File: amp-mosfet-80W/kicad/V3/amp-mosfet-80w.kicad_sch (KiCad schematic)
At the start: 60 parts, among them J1 Conn_01x01, J2 Conn_01x01, J3 +50V, J4 -50V, J5 LS+, J6 LS-, J7 GND, Q1 BC856BS, Q11 ECX10P20, Q12 ECX10N20, Q2 BC856BS, Q3 DZT5551, Q4 DZT5401, Q5 DZT5401, Q6 DZT5551

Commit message: WIP
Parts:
- removed C17: 470p, Capacitor_SMD:C_0805_2012Metric_Pad1.18x1.45mm_HandSolder, symbol Device:C
- removed Q3: DZT5551, Package_TO_SOT_SMD:SOT-223-3_TabPin2, symbol kicad-snk:DZT5551
- removed Q4: DZT5401, Package_TO_SOT_SMD:SOT-223-3_TabPin2, symbol kicad-snk:DZT5401
- added Q3: BC856BS, Package_TO_SOT_SMD:SOT-363_SC-70-6, symbol Transistor_BJT:BC856BS
- added Q4: BC846BDW1, Package_TO_SOT_SMD:SOT-363_SC-70-6, symbol Transistor_BJT:BC846BDW1
- added Q7: BC856B, Package_TO_SOT_SMD:SOT-23, symbol Transistor_BJT:BC856
- added Q8: BC846, Package_TO_SOT_SMD:SOT-23, symbol Transistor_BJT:BC846
- added R13: 1k, Resistor_SMD:R_0805_2012Metric_Pad1.20x1.40mm_HandSolder, symbol Device:R
- added R15, R22: 100R, Resistor_SMD:R_0805_2012Metric_Pad1.20x1.40mm_HandSolder, symbol Device:R
- added R16: 22k, Resistor_SMD:R_0805_2012Metric_Pad1.20x1.40mm_HandSolder, symbol Device:R
- added R23, R24: 2.2k, Resistor_SMD:R_0805_2012Metric_Pad1.20x1.40mm_HandSolder, symbol Device:R
- added R25: 33R, Resistor_SMD:R_0805_2012Metric_Pad1.20x1.40mm_HandSolder, symbol Device:R
- C1: value 2.2uF -> 3.3uF
- C3: value 10n -> 47p; footprint Capacitor_THT:C_Rect_L7.2mm_W2.5mm_P5.00mm_FKS2_FKP2_MKS2_MKP2 -> Capacitor_SMD:C_0805_2012Metric_Pad1.18x1.45mm_HandSolder
- C8: value 18p -> 47p
- R12: value 100R -> 220R
- R20: value 100R -> 33R
- R4, R7: value 3k9 -> 1k
- R5: value 430R -> 220R
- R6: value 22k -> 100R
- R8: value 100R -> 1k
- R9: value 12k/1W -> 100R; footprint Resistor_SMD:R_1206_3216Metric_Pad1.30x1.75mm_HandSolder -> Resistor_SMD:R_0805_2012Metric_Pad1.20x1.40mm_HandSolder
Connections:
- net GND: now also Q7.3 (C), R16.2
- net at C2.1, Q1.2 (B1), R2.1: now also Q3.5 (B2)
- net at Q2.6 (C1), R6.1: now also R22.1
- net at Q1.1 (E1), R6.2: no longer Q1.4 (E2)
- net at C11.1, C9.1, Q2.4 (E2)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: now also R8.2, R13.2, R23.1; no longer R8.1
- net at C5.2, Q1.5 (B2), R10.1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: now also Q3.2 (B1)
- net at C10.2, C12.2, R18.2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: now also R12.1, Q4.4 (E2), R24.2, R25.2; no longer R12.2
- net at Q1.6 (C1), R4.1: now also C8.2, Q8.1 (B); no longer C8.1, Q6.1 (B)
- net at C3.2: now also R8.1, Q3.3 (C2), Q7.1 (B); no longer R9.2
- net at C7.2, D1.2 (A), Q5.2 (C)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: now also C3.1
- net at C7.1, D4.2 (A), Q6.2 (C)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: now also C8.1; no longer C8.2
- net at Q6.3 (E): now also R25.1; no longer R12.1
- new net: Q1.4 (E2), R22.2
- new net: Q5.1 (B), Q7.2 (E), R23.2
- new net: Q6.1 (B), Q8.2 (E), R24.1
- new net: Q3.1 (E1), R15.2
- new net: Q3.6 (C1), R13.1
- new net: Q4.2 (B1), Q4.3 (C2), R16.1
- new net: Q4.1 (E1), Q4.5 (B2), R12.2
- new net: Q3.4 (E2), R9.2
- new net: Q4.6 (C1), R15.1, R9.1
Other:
- note added: "I:3.1MA"
- note removed: "C17: do not populate"
- note removed: "I:1.7mA = > 430R"
- moved on the sheet: C10, C11, C12, C13, C14, C18, C4, C5, C6, C7, C9, D1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

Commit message: WIP
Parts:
- removed JP1, JP2: Jump, Connector_PinHeader_2.54mm:PinHeader_1x02_P2.54mm_Vertical, symbol Jumper:Jumper_2_Bridged
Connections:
- net GND: now also Q8.3 (C)
- net at D5.2 (A): now also C14.1, J3.1 (Pin_1), Q12.3 (D)
- net at C18.2, J4.1 (Pin_1), Q11.3 (S): now also D6.1 (K)
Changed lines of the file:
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@@
     (stroke (width 0) (type default) (color 0 0 0 0))
   )
-  (wire (pts (xy 317.5 217.17) (xy 335.28 217.17))
+  (wire (pts (xy 306.07 217.17) (xy 335.28 217.17))
     (stroke (width 0) (type default) (color 0 0 0 0))
   )
@@
     (stroke (width 0) (type default) (color 0 0 0 0))
   )
+  (wire (pts (xy 237.49 179.07) (xy 237.49 180.34))
+    (stroke (width 0) (type default) (color 0 0 0 0))
+  )
   (wire (pts (xy 287.02 58.42) (xy 287.02 60.96))
     (stroke (width 0) (type default) (color 0 0 0 0))
@@
     (stroke (width 0) (type default) (color 0 0 0 0))
   )
-  (wire (pts (xy 306.07 58.42) (xy 307.34 58.42))
-    (stroke (width 0) (type default) (color 0 0 0 0))
-  )
   (wire (pts (xy 248.92 166.37) (xy 248.92 171.45))
     (stroke (width 0) (type default) (color 0 0 0 0))
@@
     (stroke (width 0) (type default) (color 0 0 0 0))
   )
-  (wire (pts (xy 317.5 58.42) (xy 335.28 58.42))
+  (wire (pts (xy 306.07 58.42) (xy 335.28 58.42))
     (stroke (width 0) (type default) (color 0 0 0 0))
   )
@@
   )
   (wire (pts (xy 165.1 151.13) (xy 165.1 149.86))
-    (stroke (width 0) (type default) (color 0 0 0 0))
-  )
-  (wire (pts (xy 307.34 217.17) (xy 306.07 217.17))
     (stroke (width 0) (type default) (color 0 0 0 0))
   )
@@
     (pin "1")
   )
-  (symbol (lib_id "Jumper:Jumper_2_Bridged") (at 312.42 58.42 0) (unit 1)
-    (in_bom yes) (on_board yes)
-    (property "Reference" "JP1" (id 0) (at 312.42 53.467 0))
-    (property "Value" "Jump" (id 1) (at 312.42 55.7784 0))
-    (property "Footprint" "Connector_PinHeader_2.54mm:PinHeader_1x02_P2.54mm_Vertical" (id 2) (at 312.42 58.42 0)
-      (effects (font (size 1.27 1.27)) hide)
-    )
-    (property "Datasheet" "~" (id 3) (at 312.42 58.42 0)
-      (effects (font (size 1.27 1.27)) hide)
-    )
-    (pin "1")
-    (pin "2")
-  )
   (symbol (lib_id "Device:R") (at 156.21 64.77 0) (unit 1)
     (in_bom yes) (on_board yes)
@@
     )
     (property "Datasheet" "~" (id 3) (at 156.21 64.77 0)
-      (effects (font (size 1.27 1.27)) hide)
-    )
-    (pin "1")
-    (pin "2")
-  )
-  (symbol (lib_id "Jumper:Jumper_2_Bridged") (at 312.42 217.17 180) (unit 1)
-    (in_bom yes) (on_board yes)
-    (property "Reference" "JP2" (id 0) (at 312.42 211.455 0))
-    (property "Value" "Jump" (id 1) (at 312.42 213.7664 0))
-    (property "Footprint" "Connector_PinHeader_2.54mm:PinHeader_1x02_P2.54mm_Vertical" (id 2) (at 312.42 217.17 0)
-      (effects (font (size 1.27 1.27)) hide)
-    )
-    (property "Datasheet" "~" (id 3) (at 312.42 217.17 0)
       (effects (font (size 1.27 1.27)) hide)
     )
@@
       (reference "J7") (unit 1) (value "GND") (footprint "Connector_Wire:SolderWire-1.5sqmm_1x01_D1.7mm_OD3.9mm")
     )
-    (path "/00000000-0000-0000-0000-000061924f3d"
-      (reference "JP1") (unit 1) (value "Jump") (footprint "Connector_PinHeader_2.54mm:PinHeader_1x02_P2.54mm_Vertical")
-    )
-    (path "/00000000-0000-0000-0000-000061925756"
-      (reference "JP2") (unit 1) (value "Jump") (footprint "Connector_PinHeader_2.54mm:PinHeader_1x02_P2.54mm_Vertical")
-    )
     (path "/00000000-0000-0000-0000-00006196da4b"

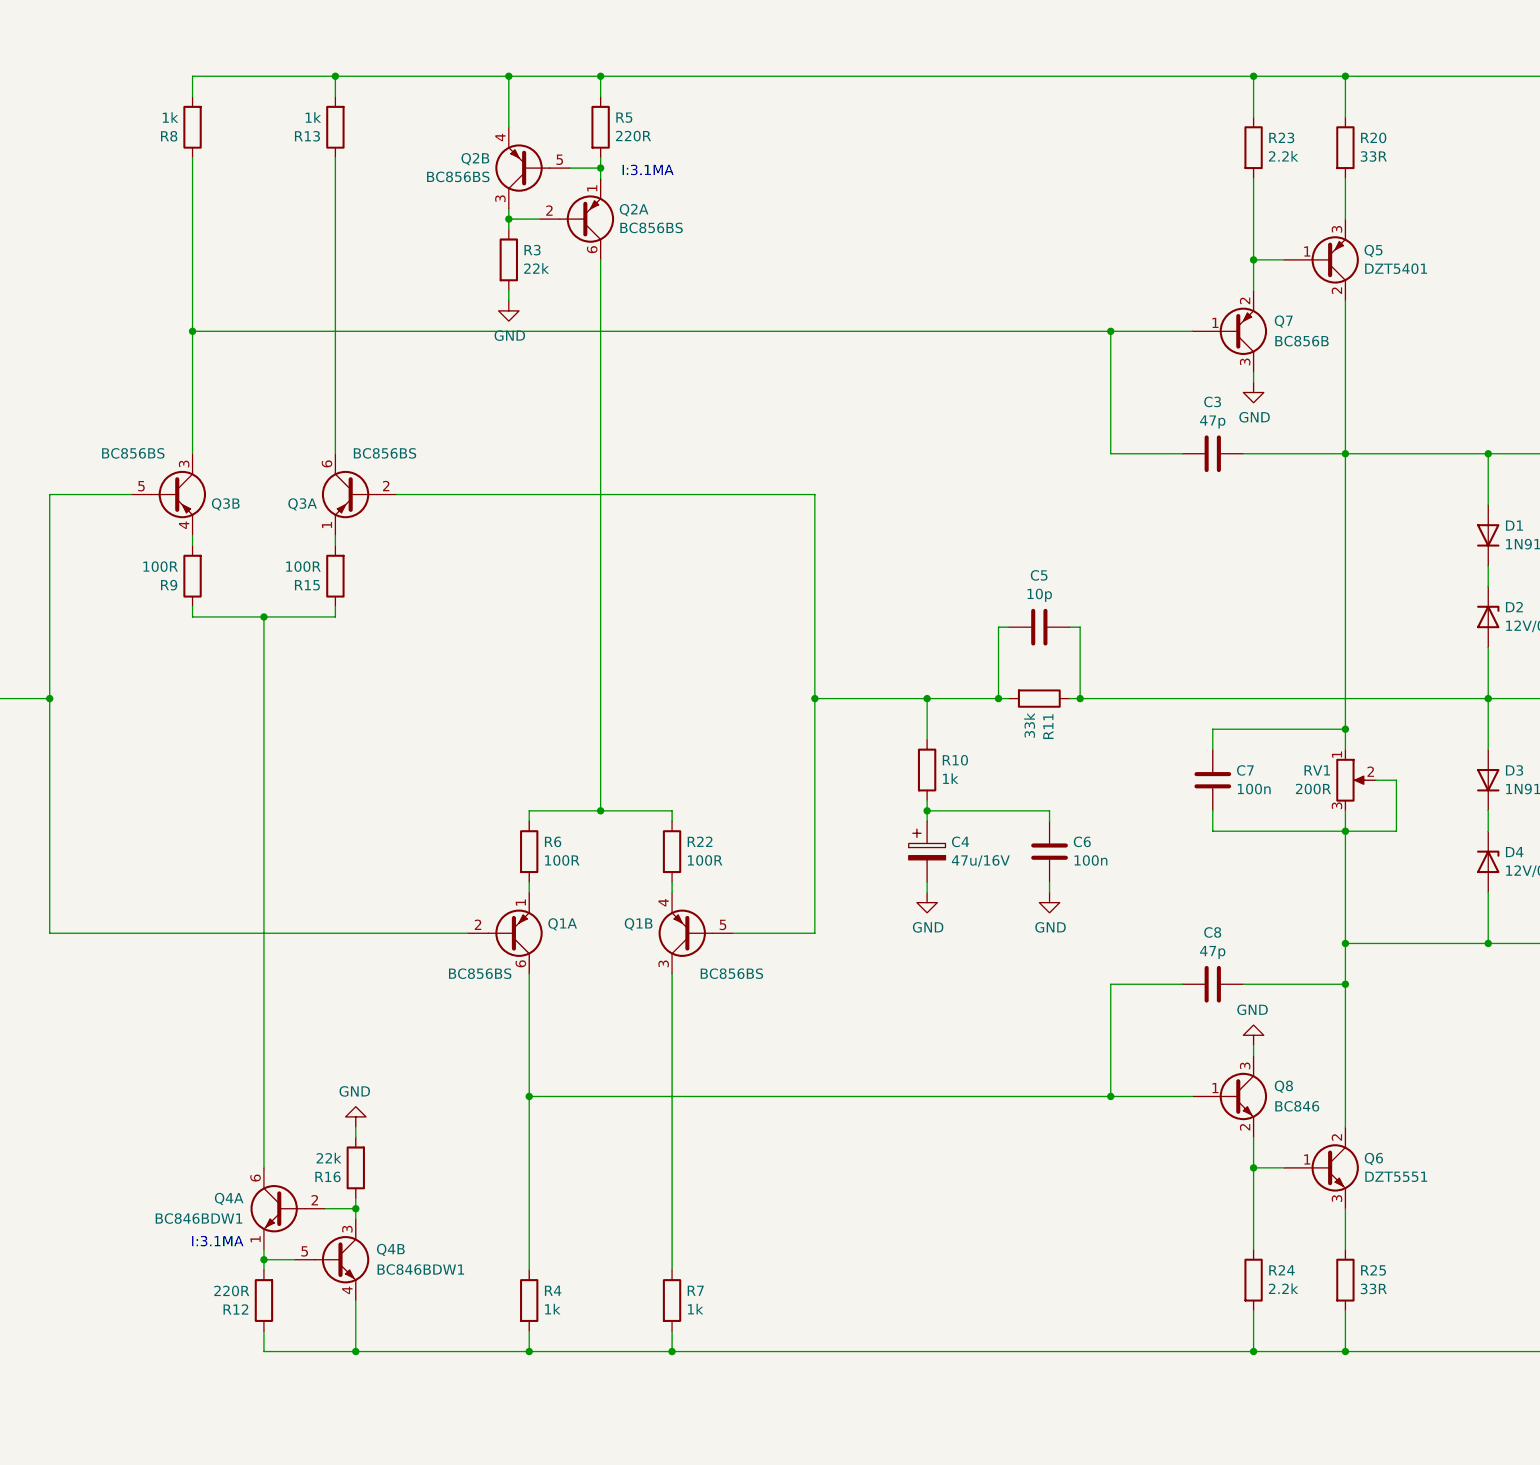
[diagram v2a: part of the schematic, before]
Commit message: Update amp-mosfet-80w.kicad_sch
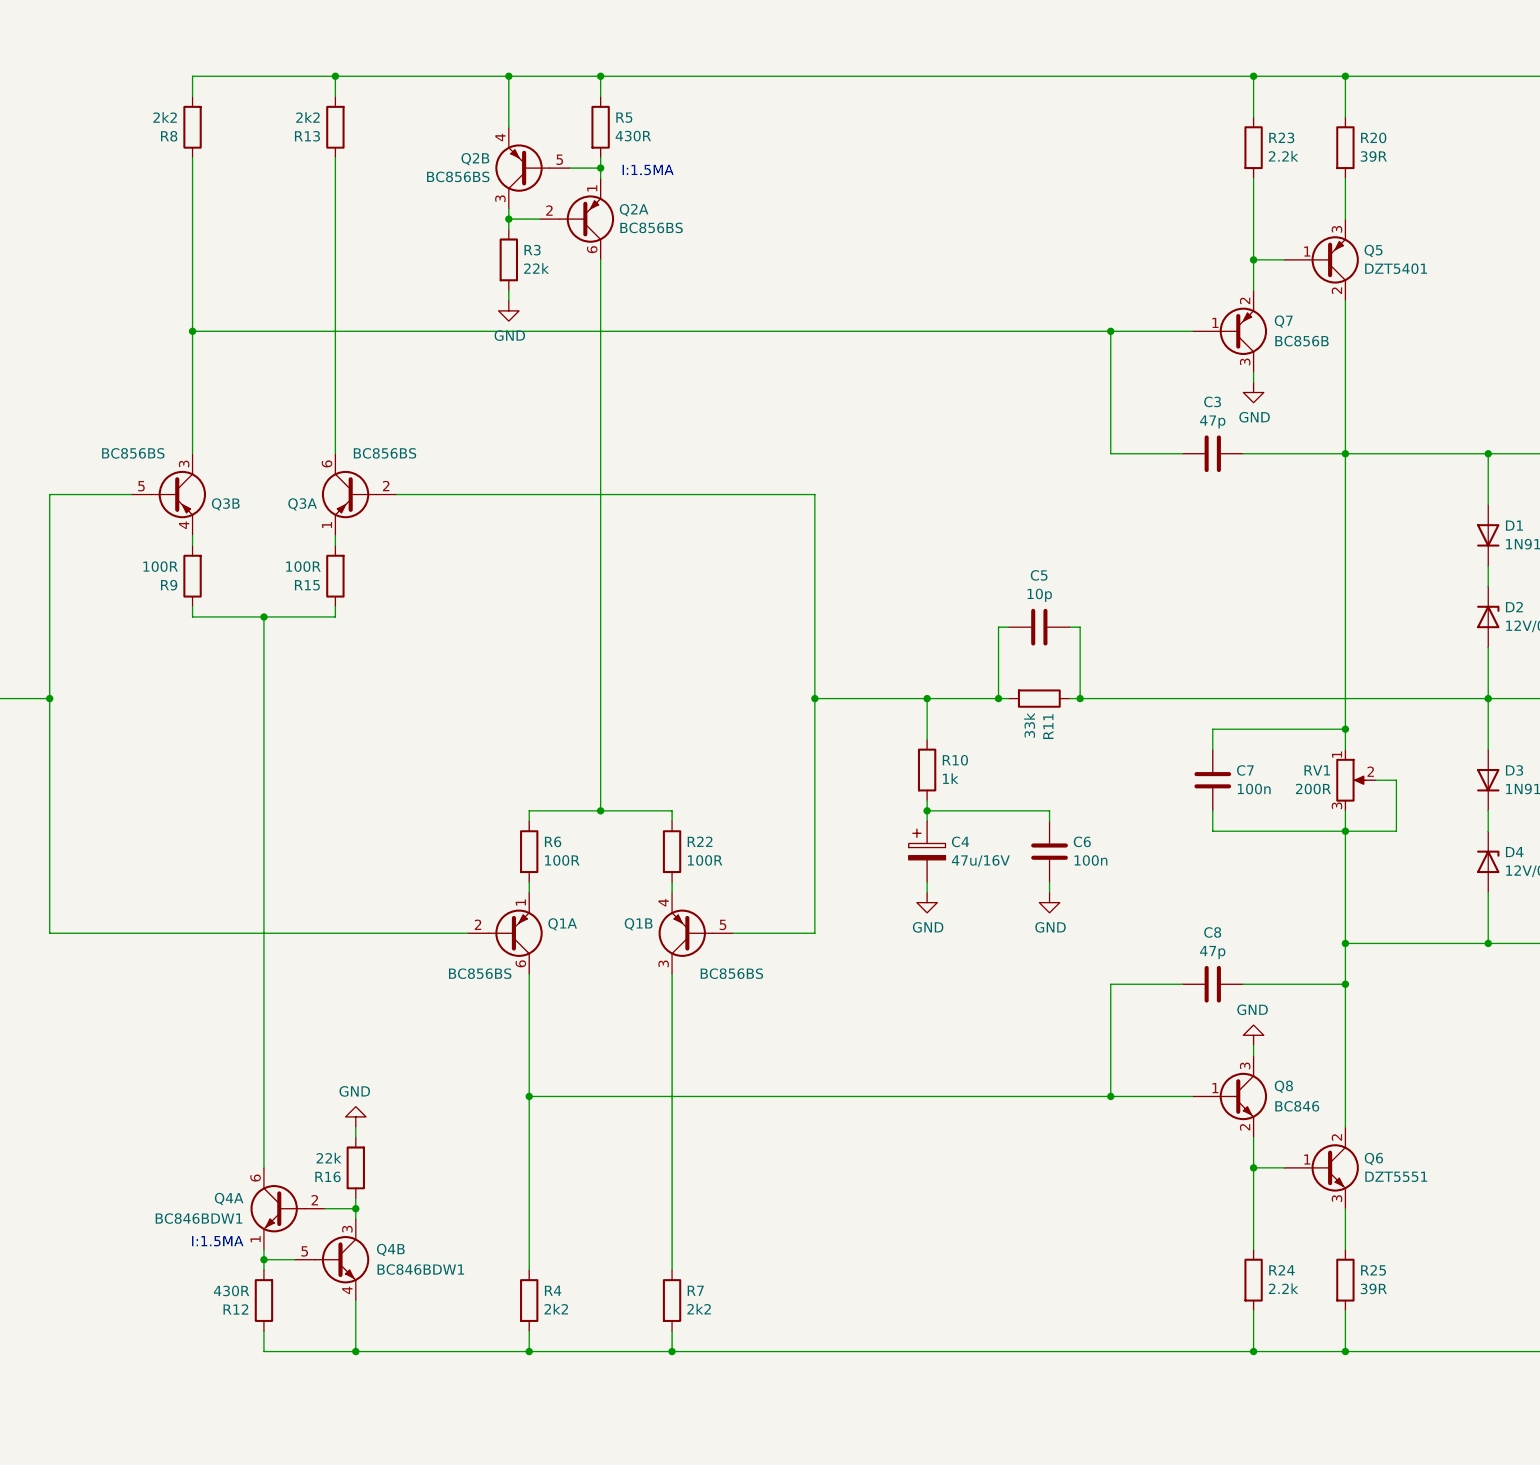
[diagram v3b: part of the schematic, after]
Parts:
- R12, R5: value 220R -> 430R
- R13, R4, R7, R8: value 1k -> 2k2
- R20, R25: value 33R -> 39R
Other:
- note added: "I:1.5MA"
- note removed: "I:3.1MA"
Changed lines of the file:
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@@
   (title_block
     (title "Lateral MOS FET 80W")
-    (date "2021-12-30")
+    (date "2022-01-07")
     (rev "V3")
   )
@@
     (stroke (width 0) (type default) (color 0 0 0 0))
   )
-  (text "I:3.1MA" (at 111.76 204.47 180)
+  (text "I:1.5MA" (at 111.76 204.47 180)
     (effects (font (size 1.27 1.27)) (justify right bottom))
   )
@@
     (effects (font (size 1.27 1.27)) (justify left bottom))
   )
-  (text "I:3.1MA" (at 158.75 71.12 0)
+  (text "I:1.5MA" (at 158.75 71.12 0)
     (effects (font (size 1.27 1.27)) (justify left bottom))
   )
@@
       (effects (font (size 1.27 1.27)) (justify left))
     )
-    (property "Value" "220R" (id 1) (at 157.988 65.913 0)
+    (property "Value" "430R" (id 1) (at 157.988 65.913 0)
       (effects (font (size 1.27 1.27)) (justify left))
     )
@@
       (effects (font (size 1.27 1.27)) (justify left))
     )
-    (property "Value" "1k" (id 1) (at 166.878 211.963 0)
+    (property "Value" "2k2" (id 1) (at 166.878 211.963 0)
       (effects (font (size 1.27 1.27)) (justify left))
     )
@@
       (effects (font (size 1.27 1.27)) (justify left))
     )
-    (property "Value" "1k" (id 1) (at 149.098 211.963 0)
+    (property "Value" "2k2" (id 1) (at 149.098 211.963 0)
       (effects (font (size 1.27 1.27)) (justify left))
     )
@@
       (effects (font (size 1.27 1.27)) (justify left))
     )
-    (property "Value" "33R" (id 1) (at 250.698 68.453 0)
+    (property "Value" "39R" (id 1) (at 250.698 68.453 0)
       (effects (font (size 1.27 1.27)) (justify left))
     )
@@
       (effects (font (size 1.27 1.27)) (justify left))
     )
-    (property "Value" "33R" (id 1) (at 250.698 209.423 0)
+    (property "Value" "39R" (id 1) (at 250.698 209.423 0)
       (effects (font (size 1.27 1.27)) (justify left))
     )
@@
       (effects (font (size 1.27 1.27)) (justify left))
     )
-    (property "Value" "1k" (id 1) (at 121.412 63.627 0)
+    (property "Value" "2k2" (id 1) (at 121.412 63.627 0)
       (effects (font (size 1.27 1.27)) (justify left))
     )
@@
       (effects (font (size 1.27 1.27)) (justify left))
     )
-    (property "Value" "1k" (id 1) (at 103.632 63.627 0)
+    (property "Value" "2k2" (id 1) (at 103.632 63.627 0)
       (effects (font (size 1.27 1.27)) (justify left))
     )
@@
       (effects (font (size 1.27 1.27)) (justify left))
     )
-    (property "Value" "220R" (id 1) (at 112.522 209.677 0)
+    (property "Value" "430R" (id 1) (at 112.522 209.677 0)
       (effects (font (size 1.27 1.27)) (justify left))
     )
@@
     )
     (path "/00000000-0000-0000-0000-000061935443"
-      (reference "R4") (unit 1) (value "1k") (footprint "Resistor_SMD:R_0805_2012Metric_Pad1.20x1.40mm_HandSolder")
+      (reference "R4") (unit 1) (value "2k2") (footprint "Resistor_SMD:R_0805_2012Metric_Pad1.20x1.40mm_HandSolder")
     )
     (path "/00000000-0000-0000-0000-00006192531f"
-      (reference "R5") (unit 1) (value "220R") (footprint "Resistor_SMD:R_0805_2012Metric_Pad1.20x1.40mm_HandSolder")
+      (reference "R5") (unit 1) (value "430R") (footprint "Resistor_SMD:R_0805_2012Metric_Pad1.20x1.40mm_HandSolder")
     )
     (path "/00000000-0000-0000-0000-00006191f500"
@@
     )
     (path "/00000000-0000-0000-0000-000061934148"
-      (reference "R7") (unit 1) (value "1k") (footprint "Resistor_SMD:R_0805_2012Metric_Pad1.20x1.40mm_HandSolder")
+      (reference "R7") (unit 1) (value "2k2") (footprint "Resistor_SMD:R_0805_2012Metric_Pad1.20x1.40mm_HandSolder")
     )
     (path "/bc4f73f6-106f-4cc8-bb82-bc8efa1afc3e"
-      (reference "R8") (unit 1) (value "1k") (footprint "Resistor_SMD:R_0805_2012Metric_Pad1.20x1.40mm_HandSolder")
+      (reference "R8") (unit 1) (value "2k2") (footprint "Resistor_SMD:R_0805_2012Metric_Pad1.20x1.40mm_HandSolder")
     )
     (path "/df83a6e7-4009-4e15-8848-71fca1944547"
@@
     )
     (path "/cc4b2573-d454-4623-b5a2-500c7c0c1f4f"
-      (reference "R12") (unit 1) (value "220R") (footprint "Resistor_SMD:R_0805_2012Metric_Pad1.20x1.40mm_HandSolder")
+      (reference "R12") (unit 1) (value "430R") (footprint "Resistor_SMD:R_0805_2012Metric_Pad1.20x1.40mm_HandSolder")
     )
     (path "/6a7d600b-c6ab-4f20-9356-09f2372162be"
-      (reference "R13") (unit 1) (value "1k") (footprint "Resistor_SMD:R_0805_2012Metric_Pad1.20x1.40mm_HandSolder")
+      (reference "R13") (unit 1) (value "2k2") (footprint "Resistor_SMD:R_0805_2012Metric_Pad1.20x1.40mm_HandSolder")
     )
     (path "/00000000-0000-0000-0000-00006195ccda"
@@
     )
     (path "/00000000-0000-0000-0000-0000619d631c"
-      (reference "R20") (unit 1) (value "33R") (footprint "Resistor_SMD:R_0805_2012Metric_Pad1.20x1.40mm_HandSolder")
+      (reference "R20") (unit 1) (value "39R") (footprint "Resistor_SMD:R_0805_2012Metric_Pad1.20x1.40mm_HandSolder")
     )
     (path "/00000000-0000-0000-0000-0000619c33bd"
@@
     )
     (path "/0e2a06e4-cc58-4232-9eb1-d0f4b74d3202"
-      (reference "R25") (unit 1) (value "33R") (footprint "Resistor_SMD:R_0805_2012Metric_Pad1.20x1.40mm_HandSolder")
+      (reference "R25") (unit 1) (value "39R") (footprint "Resistor_SMD:R_0805_2012Metric_Pad1.20x1.40mm_HandSolder")
     )
     (path "/00000000-0000-0000-0000-00006194c763"
